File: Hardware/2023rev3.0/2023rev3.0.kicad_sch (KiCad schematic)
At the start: 109 parts

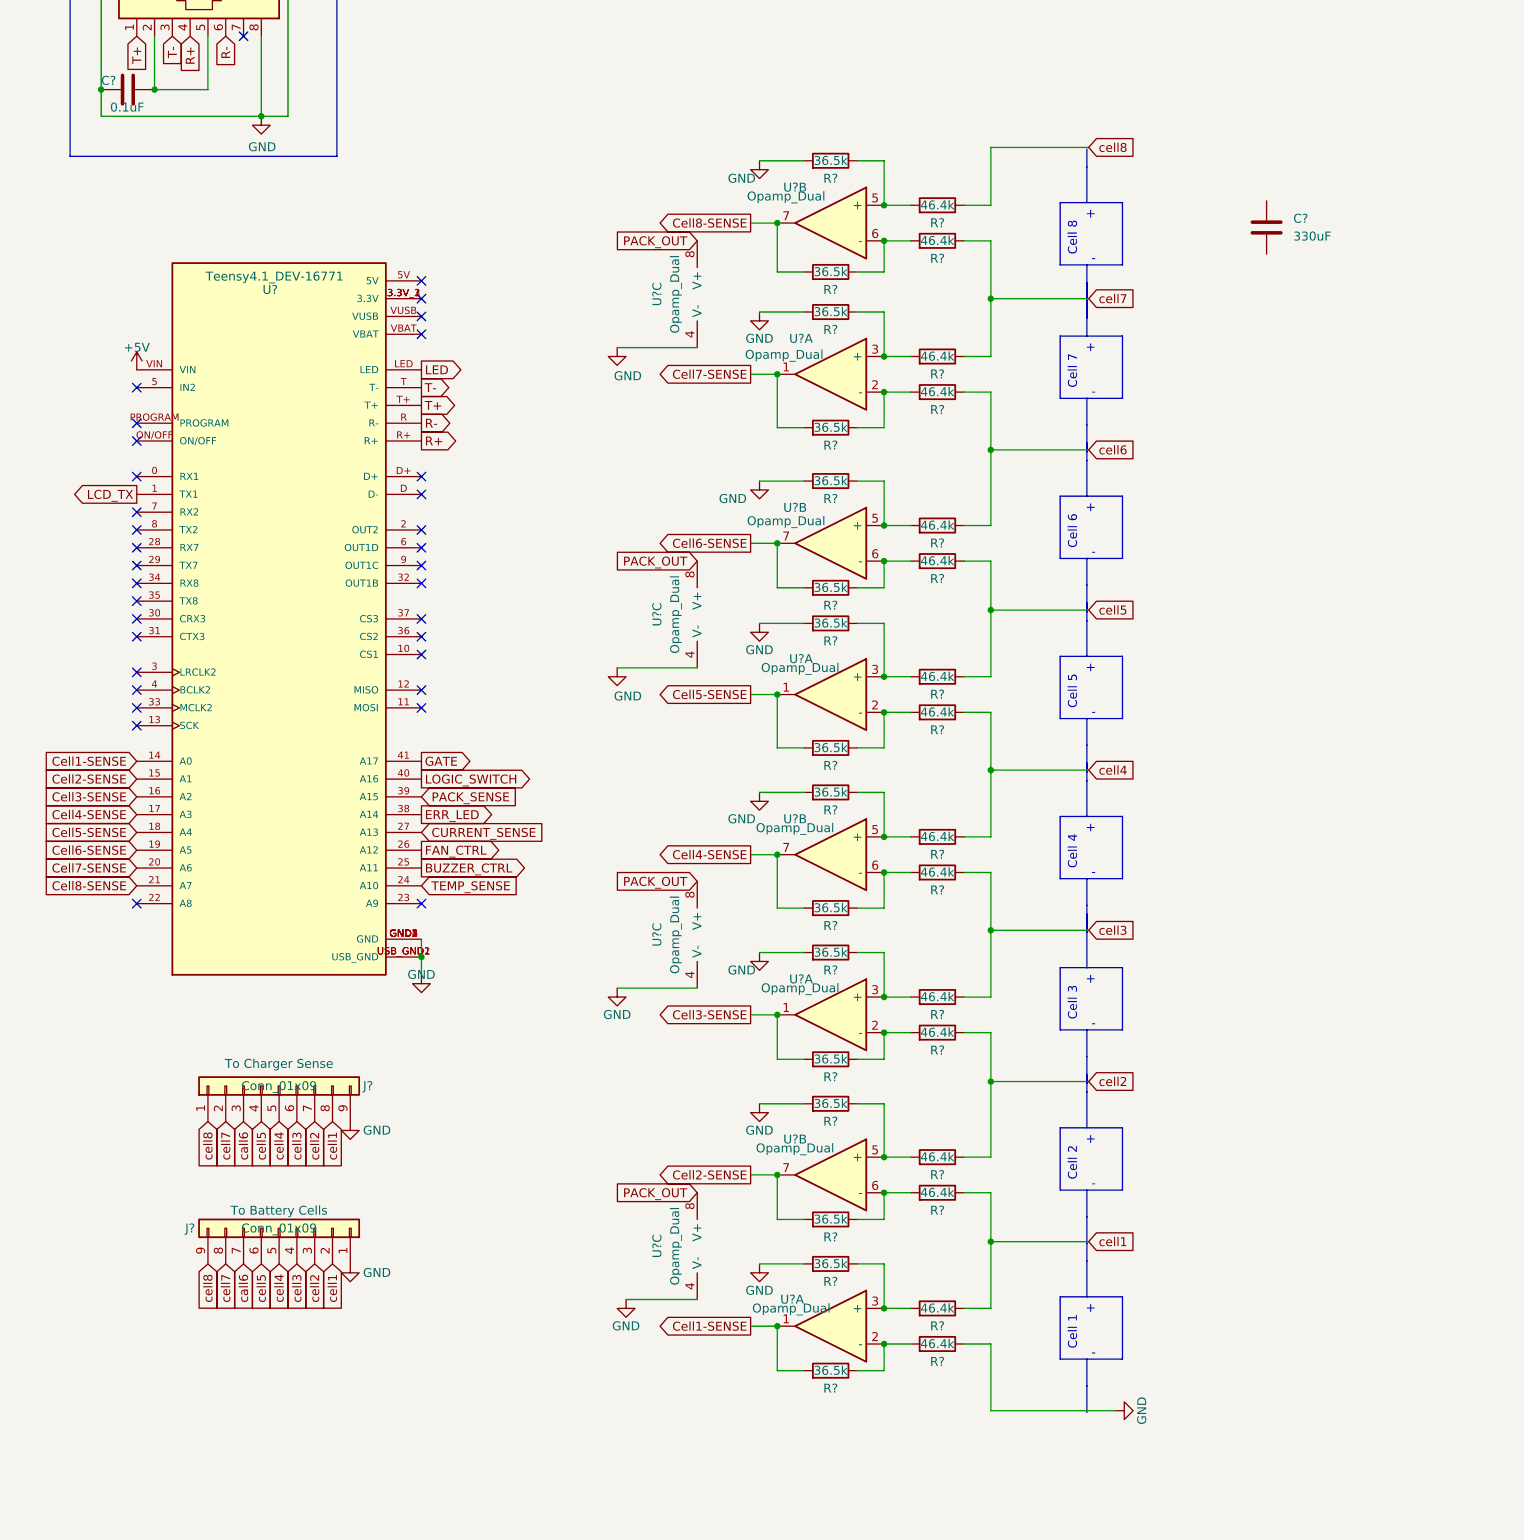
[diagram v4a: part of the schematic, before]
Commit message: Added caps and switches with footprint
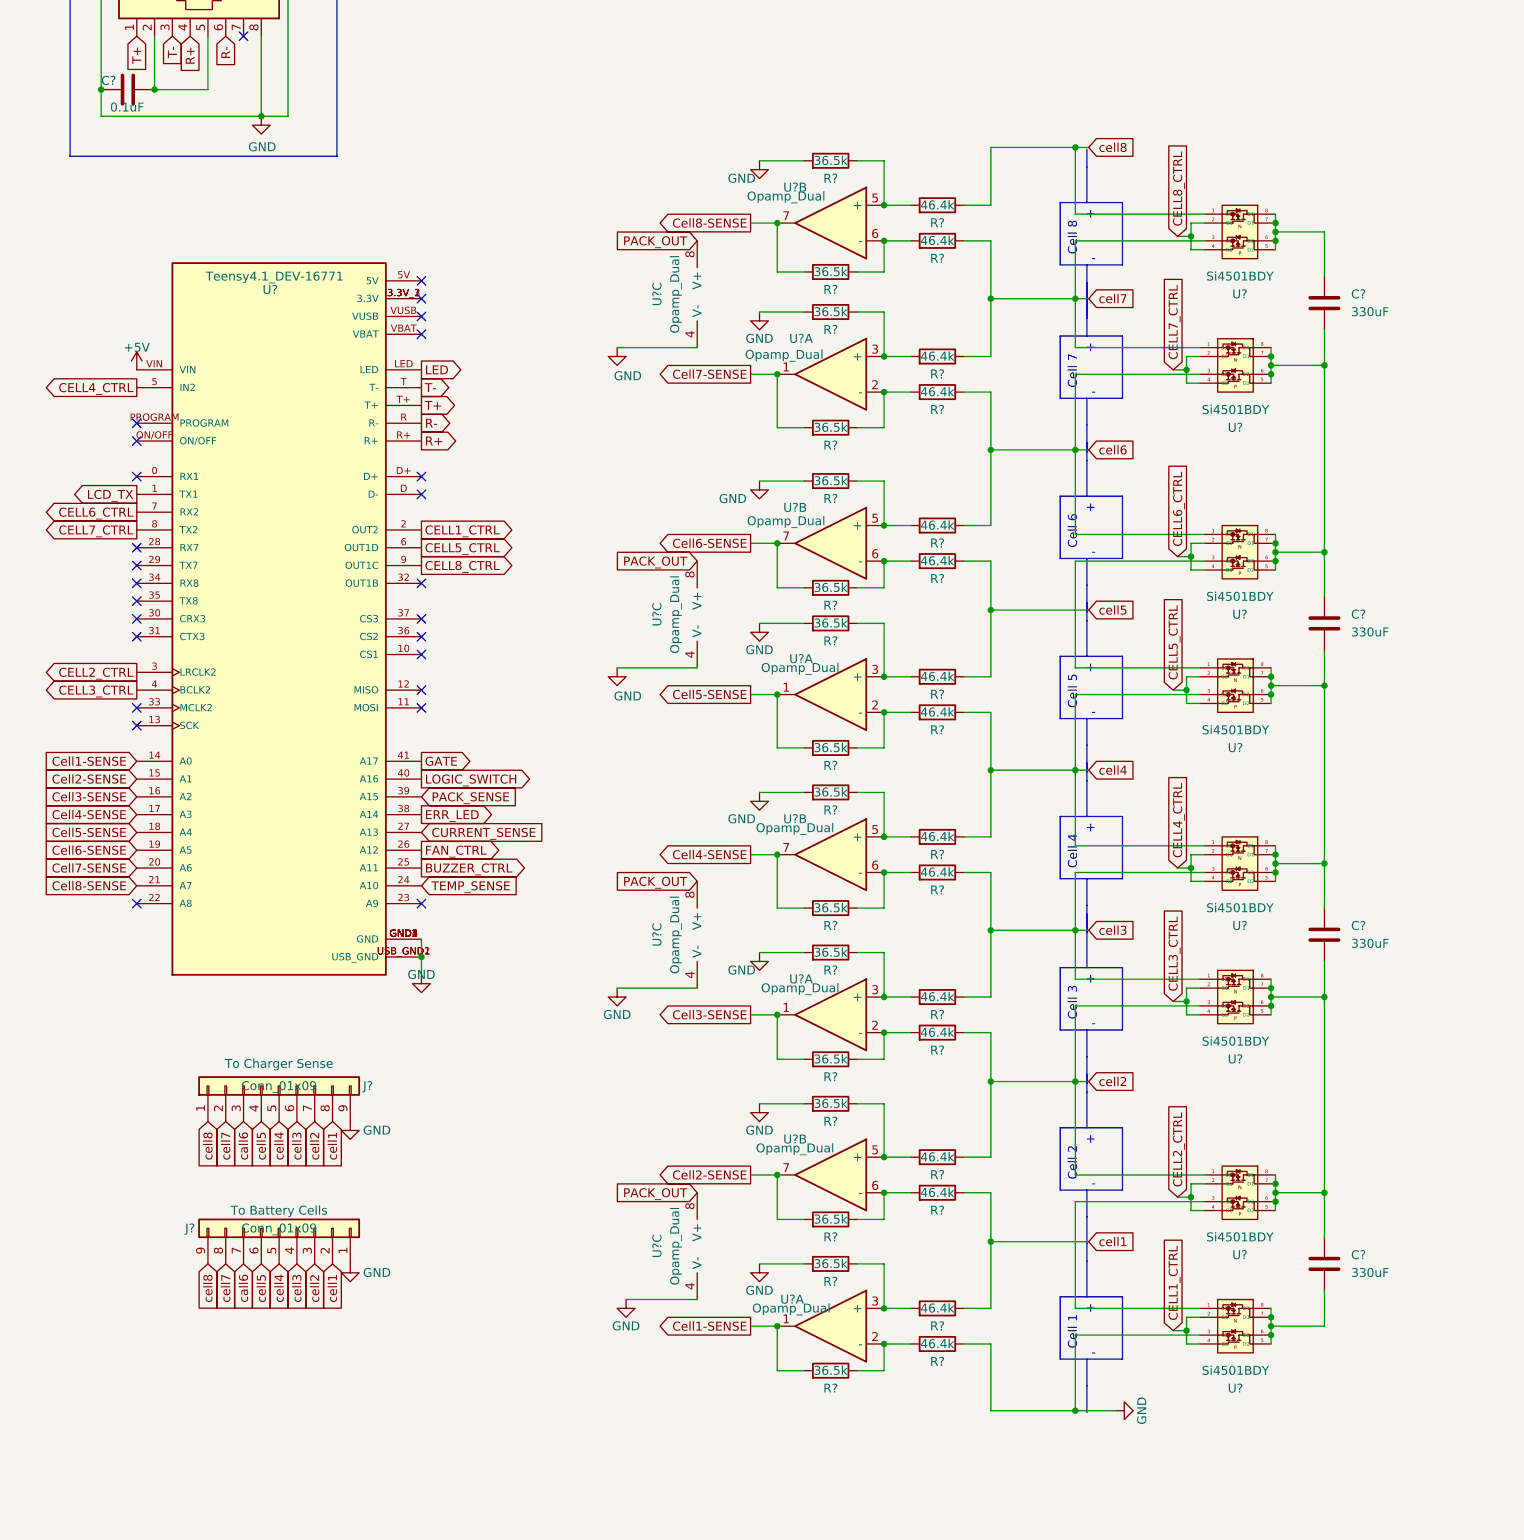
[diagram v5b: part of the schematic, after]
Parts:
- added C? (x3): 330uF, symbol Device:C
- added U? (x8): Si4501BDY, symbol MRDT_Devices:Si4501BDY
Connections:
- net GND: now also U?.3 (S2)
- net cell2: now also U?.1 (S1), U?.3 (S2)
- net cell3: now also U?.1 (S1), U?.3 (S2)
- net cell4: now also U?.1 (S1), U?.3 (S2)
- net cell6: now also U?.1 (S1), U?.3 (S2)
- net cell7: now also U?.1 (S1), U?.3 (S2)
- net cell8: now also U?.1 (S1)
- net CELL1_CTRL: now reaches U?.2 (OUT2)
- net CELL1_CTRL: now also U?.2 (G1), U?.4 (G2)
- net CELL2_CTRL: now reaches U?.3 (LRCLK2)
- net CELL2_CTRL: now also U?.2 (G1), U?.4 (G2)
- net CELL3_CTRL: now reaches U?.4 (BCLK2)
- net CELL3_CTRL: now also U?.2 (G1), U?.4 (G2)
- net CELL4_CTRL: now reaches U?.5 (IN2)
- net CELL4_CTRL: now also U?.2 (G1), U?.4 (G2)
- net CELL5_CTRL: now reaches U?.6 (OUT1D)
- net CELL5_CTRL: now also U?.2 (G1), U?.4 (G2)
- net CELL6_CTRL: now reaches U?.7 (RX2)
- net CELL6_CTRL: now also U?.2 (G1), U?.4 (G2)
- net CELL7_CTRL: now reaches U?.8 (TX2)
- net CELL7_CTRL: now also U?.2 (G1), U?.4 (G2)
- net CELL8_CTRL: now reaches U?.9 (OUT1C)
- net CELL8_CTRL: now also U?.2 (G1), U?.4 (G2)
- net at C?.1: now also U?.5 (D2), U?.6 (D2), U?.7 (D1), U?.8 (D1)
- net at C?.2: now also C?.1, U?.5 (D2), U?.5 (D2), U?.6 (D2), U?.6 (D2), U?.7 (D1), U?.7 (D1), U?.8 (D1), U?.8 (D1)
- new net: U?.1 (S1), U?.3 (S2) (x2)
- new net: C?.1, C?.2, U?.5 (D2), U?.5 (D2), U?.6 (D2), U?.6 (D2), U?.7 (D1), U?.7 (D1), U?.8 (D1), U?.8 (D1) (x2)
- new net: C?.2, U?.5 (D2), U?.6 (D2), U?.7 (D1), U?.8 (D1)
- no-connect marks 38 -> 30
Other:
- moved on the sheet: C?

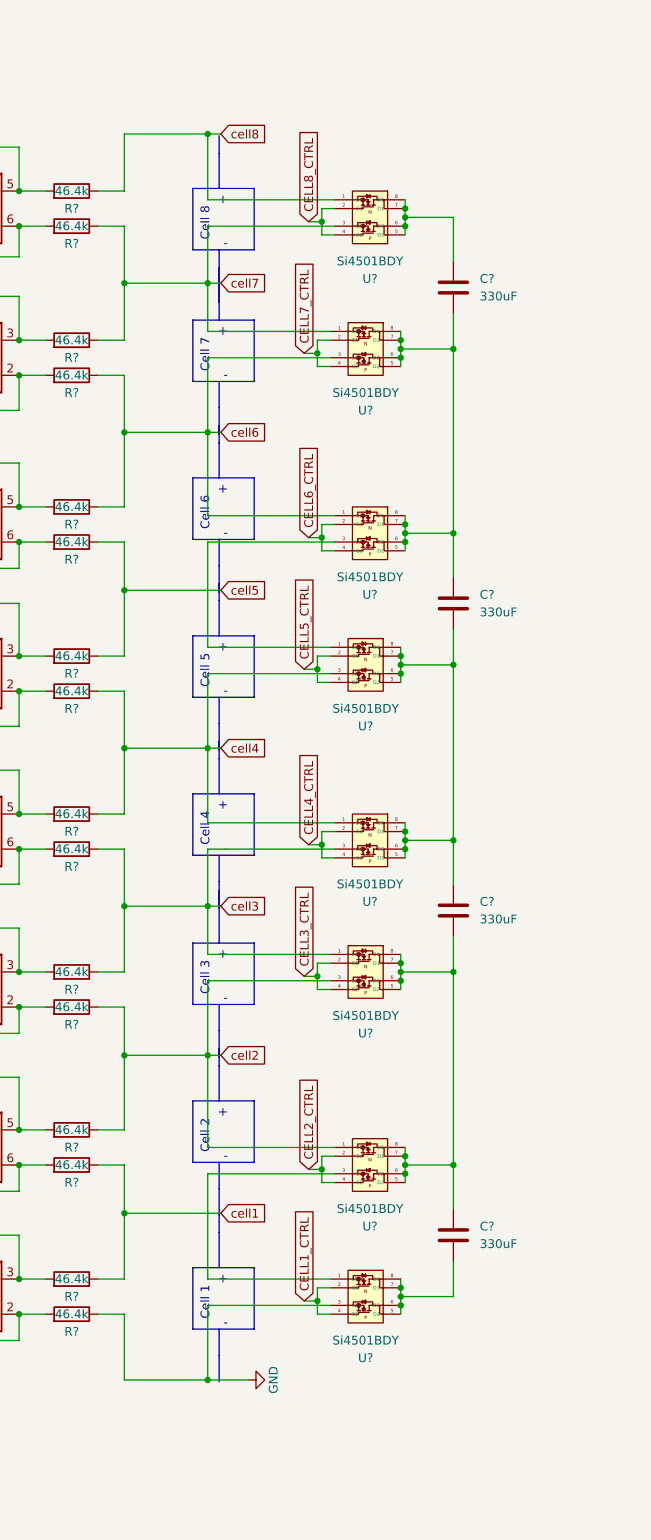
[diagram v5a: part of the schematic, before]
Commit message: Added caps for all cells
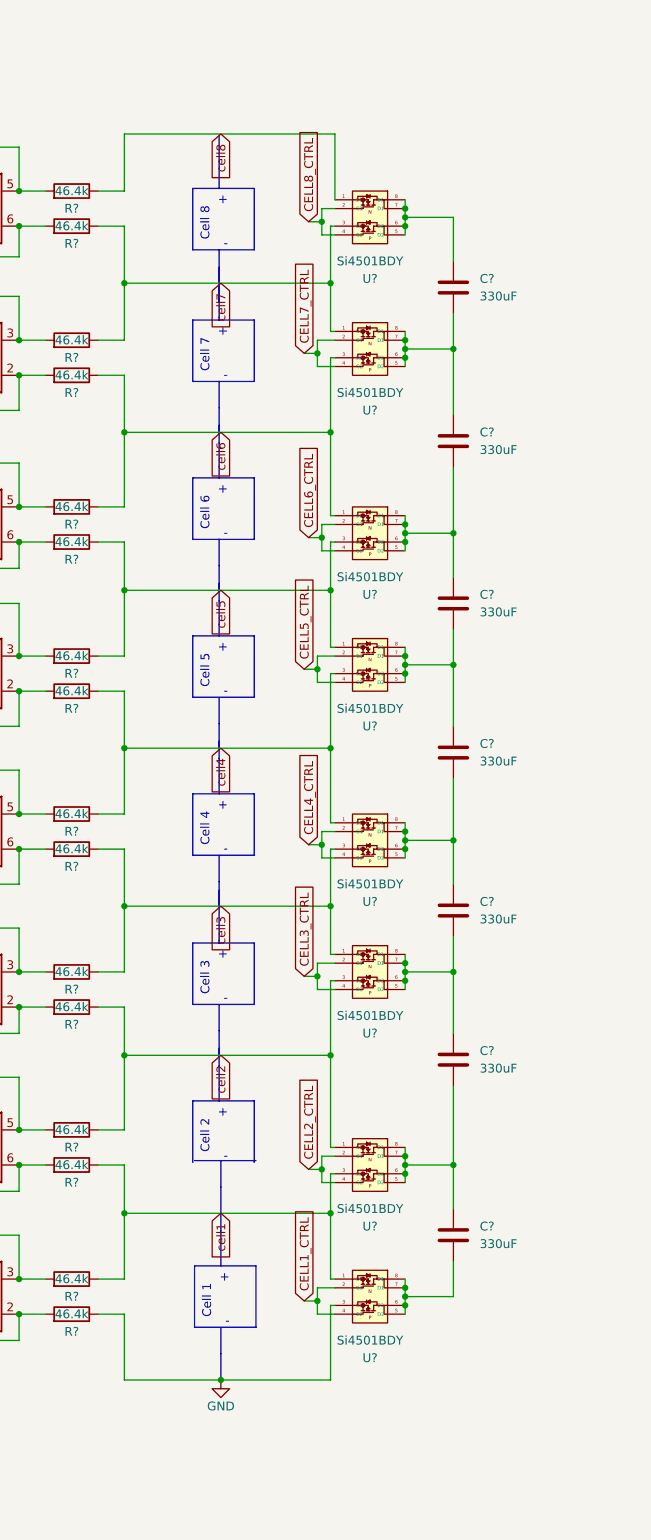
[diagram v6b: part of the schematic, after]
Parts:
- added C? (x3): 330uF, symbol Device:C
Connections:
- net cell1: now also U?.1 (S1), U?.3 (S2)
- net cell5: now also U?.1 (S1), U?.3 (S2)
- net at C?.2, U?.5 (D2), U?.6 (D2)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: now also C?.1; no longer C?.1, U?.5 (D2), U?.6 (D2), U?.7 (D1), U?.8 (D1) (x2)
- net at C?.1, U?.5 (D2), U?.6 (D2)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: now also C?.2; no longer C?.2, U?.5 (D2), U?.6 (D2), U?.7 (D1), U?.8 (D1)
- new net: C?.1, C?.2, U?.5 (D2), U?.6 (D2), U?.7 (D1), U?.8 (D1) (x3)
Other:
- moved on the sheet: U?
